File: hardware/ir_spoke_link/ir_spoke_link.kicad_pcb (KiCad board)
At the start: 2 copper layers, 21.5 x 18 mm, 14 parts, among them J1 XIAO_LEFT, J2 XIAO_RIGHT, Q1 S8050, U1 TSOP57438TT1

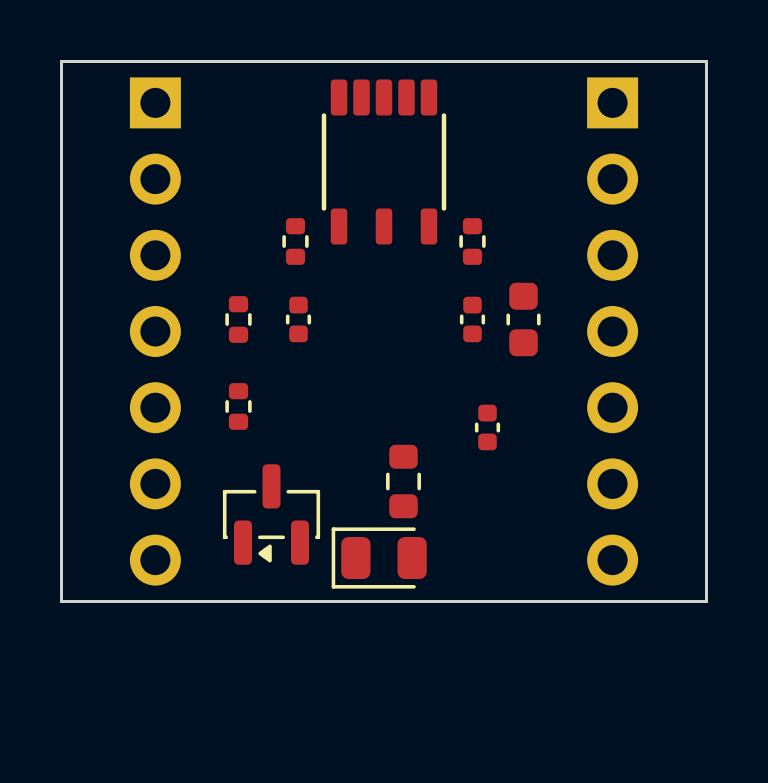
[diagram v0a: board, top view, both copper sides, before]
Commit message: Build discrete IR spoke sensor system and technical docs
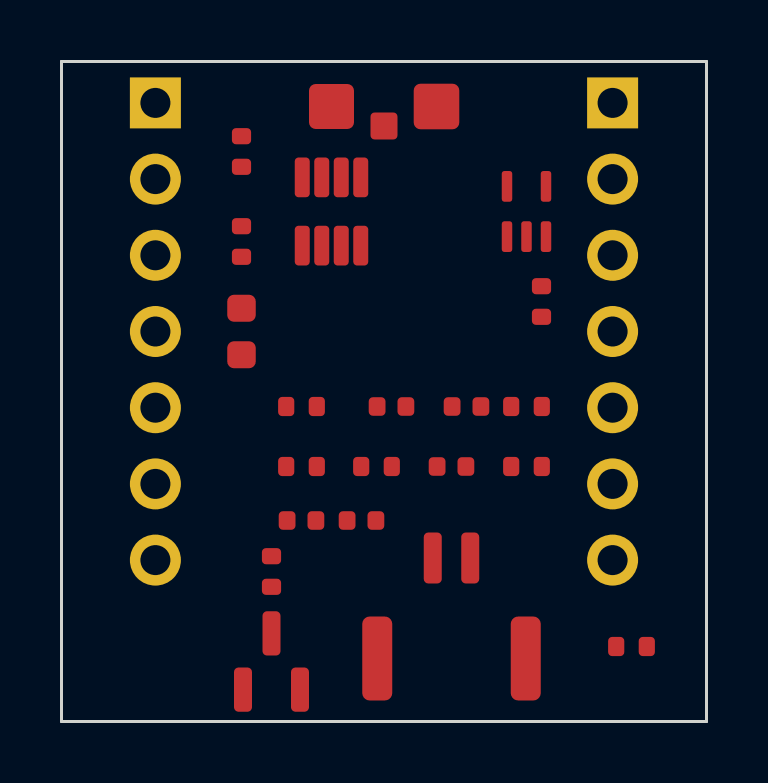
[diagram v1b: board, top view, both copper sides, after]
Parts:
- removed D1: VSMB1940X01, LED_0805_2012Metric
- removed R1: 39R, R_0603_1608Metric
- added C5: 100n, C_0402_1005Metric, F.Cu at (8.00, 15.3)
- added C6: 100n, C_0402_1005Metric, F.Cu at (10.0, 15.3)
- added D2: VEMD10940FX01, VEMD10940F_SideView, F.Cu at (10.8, 1.50)
- added J3: TX CABLE, JST_GH_BM02B-GHS-TBT_1x02-1MP_P1.25mm_Vertical, F.Cu at (13.0, 18.5)
- added R10: 1M, R_0402_1005Metric, F.Cu at (16.0, 8.00)
- added R11: 100R, R_0402_1005Metric, F.Cu at (19.0, 19.5)
- added R6: 16k, R_0402_1005Metric, F.Cu at (15.5, 11.5)
- added R7: 10k, R_0402_1005Metric, F.Cu at (8.00, 13.5)
- added R8: 100k, R_0402_1005Metric, F.Cu at (10.5, 13.5)
- added R9: 10k, R_0402_1005Metric, F.Cu at (15.5, 13.5)
- added U2: TLV7011DCKR, SOT-353_SC-70-5, F.Cu at (15.5, 5.00)
- C1: value 100n -> 1u; footprint C_0402_1005Metric -> C_0603_1608Metric
- C2: value 4.7u -> 120p; footprint C_0603_1608Metric -> C_0402_1005Metric
- C3: value 100n -> 1n
- C4: value 47p -> 27p
- R3: value 100R -> 10k
- R5: value 100R -> 33k
- U1: value TSOP57438TT1 -> TLV9062IDDFR; footprint TSOP57_Belobog_4x4mm -> SOT-23-8
- moved C1 8.80 mm to (6.00, 9.00)
- moved R3 8.26 mm to (6.00, 3.00)
- moved C4 7.07 mm to (13.0, 13.5), turned to 0 degrees
- moved R2 5.61 mm to (7.00, 17.0)
- moved C2 5.27 mm to (11.0, 11.5), turned to 0 degrees
- moved Q1 4.90 mm to (7.00, 20.0)
- moved R5 3.58 mm to (8.00, 11.5), turned to 0 degrees
- moved C3 2.91 mm to (13.5, 11.5), turned to 0 degrees
- moved U1 2.41 mm to (9.00, 5.00), turned to 90 degrees
- moved R4 1.80 mm to (6.00, 6.00)
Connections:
- net XIAO_D10_GPIO9 renamed XIAO_D10
- net XIAO_D2_GPIO3 renamed XIAO_D2
- net XIAO_D3_GPIO4 renamed XIAO_D3
- net XIAO_D4_GPIO5 renamed XIAO_D4
- net XIAO_D5_GPIO6 renamed XIAO_D5
- net XIAO_D6_GPIO43 renamed XIAO_D6
- net XIAO_D7_GPIO44 renamed XIAO_D7
- net XIAO_D8_GPIO7 renamed XIAO_D8
- net XIAO_D9_GPIO8 renamed XIAO_D9
- C1 pad 1: +3V3 -> VREF
- C2 pad 1: RX_VS_FILTERED -> TIA_OUT
- C2 pad 2: GND -> PD_ANODE
- C3 pad 1: RX_VS_FILTERED -> TIA_OUT
- C3 pad 2: GND -> BP_IN
- C4 pad 1: RX_RMT_GPIO2 -> BANDPASS
- C4 pad 2: GND -> BP_NEG
- Q1 pad 2: LED_K -> LED_K_SWITCHED
- R3 pad 2: RX_VS_FILTERED -> VREF
- R4 pad 1: +3V3 -> VREF
- R4 pad 2: RX_RAW_ACTIVE_LOW -> GND
- R5 pad 1: RX_RAW_ACTIVE_LOW -> TIA_OUT
- R5 pad 2: RX_RMT_GPIO2 -> PD_ANODE
- U1 pad 1: RX_RAW_ACTIVE_LOW -> TIA_OUT
- U1 pad 2: GND -> PD_ANODE
- U1 pad 3: GND -> VREF
- U1 pad 4: RX_VS_FILTERED -> GND
- U1 pad 5: RX_VS_FILTERED -> BP_IN
- U1 pad 6: GND -> BP_NEG
- U1 pad 7: GND -> BANDPASS
- U1 pad 8: GND -> +3V3
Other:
- board size 21.5 x 18 mm -> 21.5 x 22 mm
- board text removed: "IR SPOKE LINK"
- board text removed: "XIAO S3"

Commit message: Make IR carrier configurable and link full simulation stack
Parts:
- C4: value 27p -> 4.7p
- R8: value 100k -> 560k
